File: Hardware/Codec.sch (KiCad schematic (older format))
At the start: 11 parts, among them U301 SGTL5000XNAA3

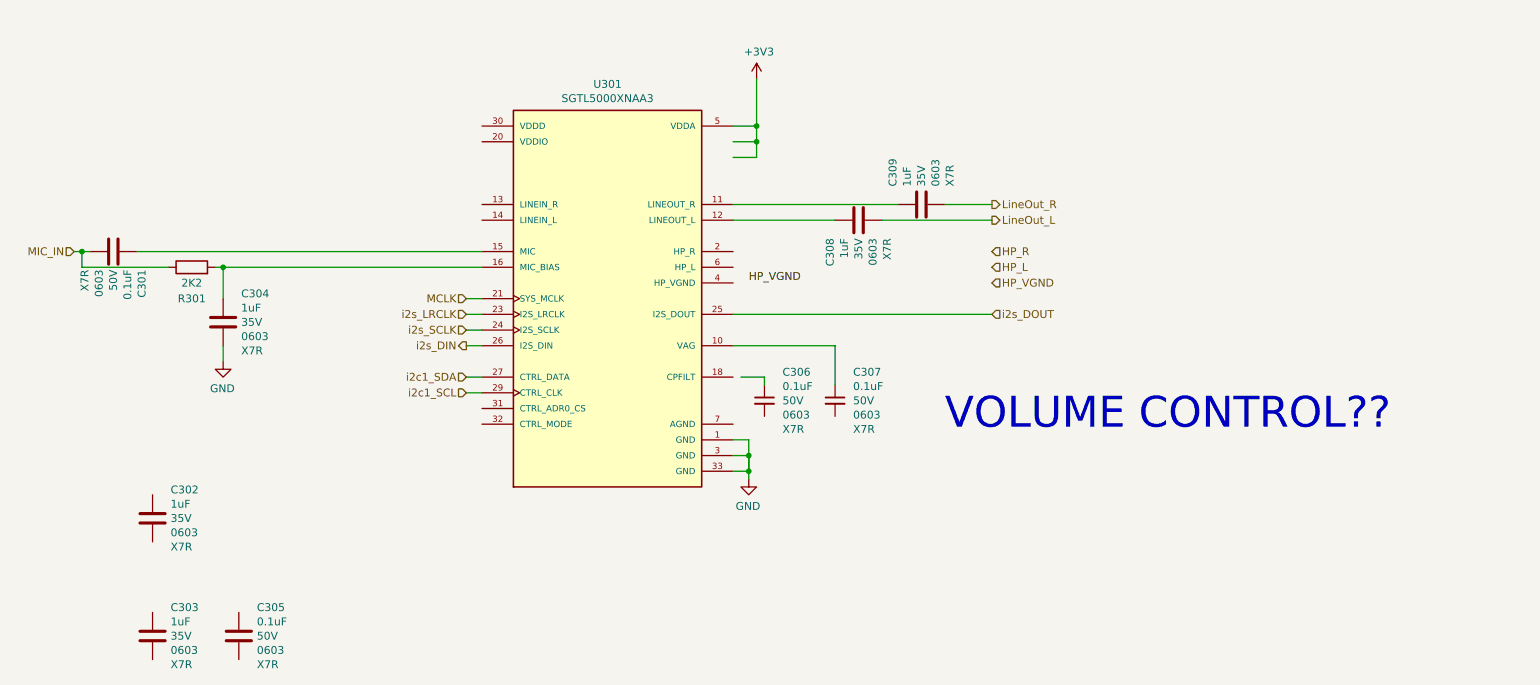
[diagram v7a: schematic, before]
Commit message: Adding in MEMS microphone library components.
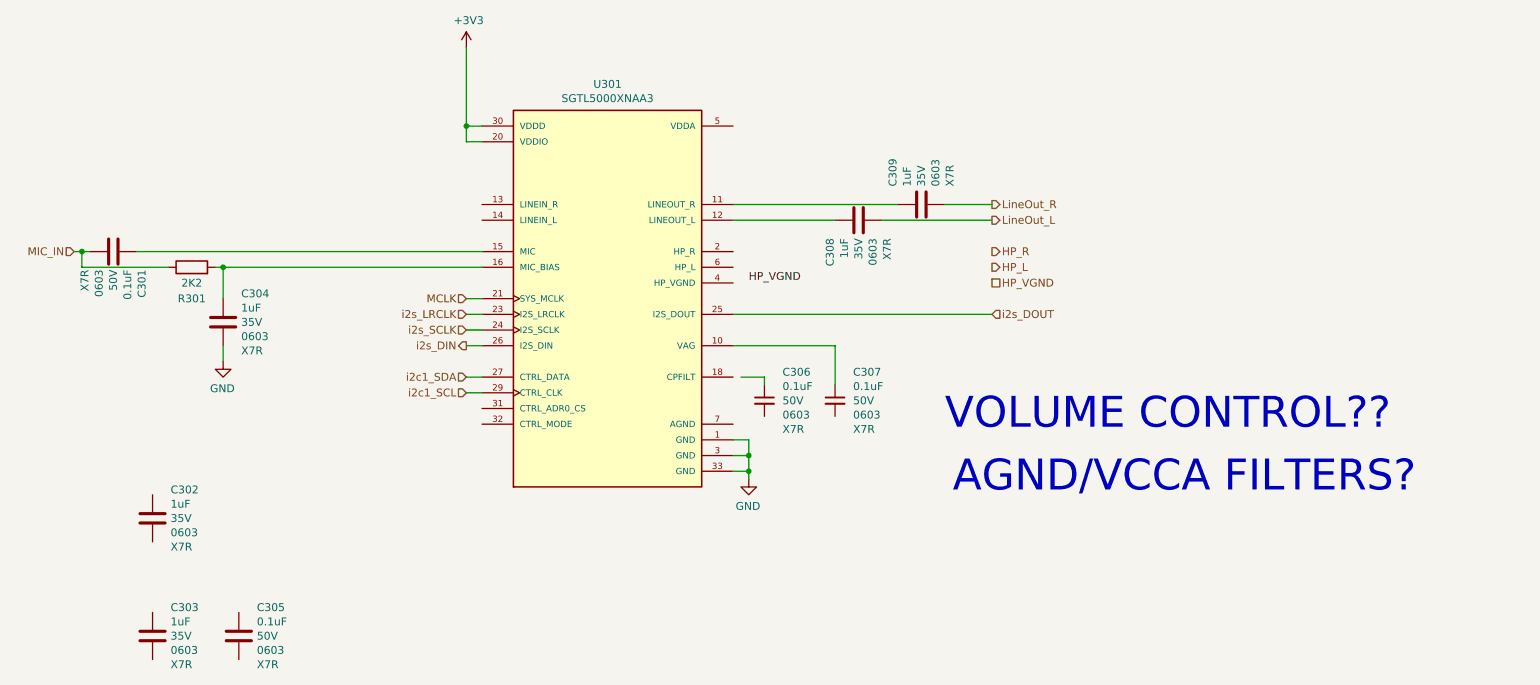
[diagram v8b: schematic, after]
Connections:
- wire segments 37 -> 34
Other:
- note added: "AGND/VCCA FILTERS?"
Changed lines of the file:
@@
 L power:+3V3 #PWR?
 U 1 1 6145BB5A
-P 6200 2050
+P 4350 1850
 AR Path="/6123BB15/6145BB5A" Ref="#PWR?"  Part="1"
 AR Path="/611E335F/6145BB5A" Ref="#PWR?"  Part="1"
 AR Path="/611E3218/611E32E1/6145BB5A" Ref="#PWR0123"  Part="1"
-F 0 "#PWR0123" H 6200 1900 50  0001 C CNN
-F 1 "+3V3" H 6215 2223 50  0000 C CNN
-F 2 "" H 6200 2050 50  0001 C CNN
-F 3 "" H 6200 2050 50  0001 C CNN
-	1    6200 2050
+F 0 "#PWR0123" H 4350 1700 50  0001 C CNN
+F 1 "+3V3" H 4365 2023 50  0000 C CNN
+F 2 "" H 4350 1850 50  0001 C CNN
+F 3 "" H 4350 1850 50  0001 C CNN
+	1    4350 1850
 	1    0    0    -1
 $EndComp
-Wire Wire Line
-	6200 2050 6200 2350
-Wire Wire Line
-	6050 2350 6200 2350
-Wire Wire Line
-	6050 2450 6200 2450
-Wire Wire Line
-	6200 2450 6200 2350
-Connection ~ 6200 2350
-Wire Wire Line
-	6050 2550 6200 2550
-Wire Wire Line
-	6200 2550 6200 2450
-Connection ~ 6200 2450
 Wire Wire Line
 	6050 3550 7700 3550
@@
 Text HLabel 1850 3150 0    50   Input ~ 0
 MIC_IN
-Text HLabel 7700 3150 2    50   Input ~ 0
+Text HLabel 7700 3150 2    50   Output ~ 0
 HP_R
-Text HLabel 7700 3250 2    50   Input ~ 0
+Text HLabel 7700 3250 2    50   Output ~ 0
 HP_L
-Text HLabel 7700 3350 2    50   Input ~ 0
+Text HLabel 7700 3350 2    50   UnSpc ~ 0
 HP_VGND
 Wire Wire Line
@@
 	6150 4350 6150 4450
 Connection ~ 6150 4450
-Wire Wire Line
-	6150 4450 6150 4550
 Text Notes 7400 4300 0    197  ~ 0
 VOLUME CONTROL??
+Wire Wire Line
+	4450 2350 4350 2350
+Wire Wire Line
+	4350 2350 4350 1850
+Wire Wire Line
+	4450 2450 4350 2450
+Wire Wire Line
+	4350 2450 4350 2350
+Connection ~ 4350 2350
+Text Notes 7450 4700 0    197  ~ 0
+AGND/VCCA FILTERS?
 $EndSCHEMATC
